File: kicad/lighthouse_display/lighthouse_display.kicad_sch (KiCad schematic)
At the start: 1 part, among them U1 IS31FL3731-SA

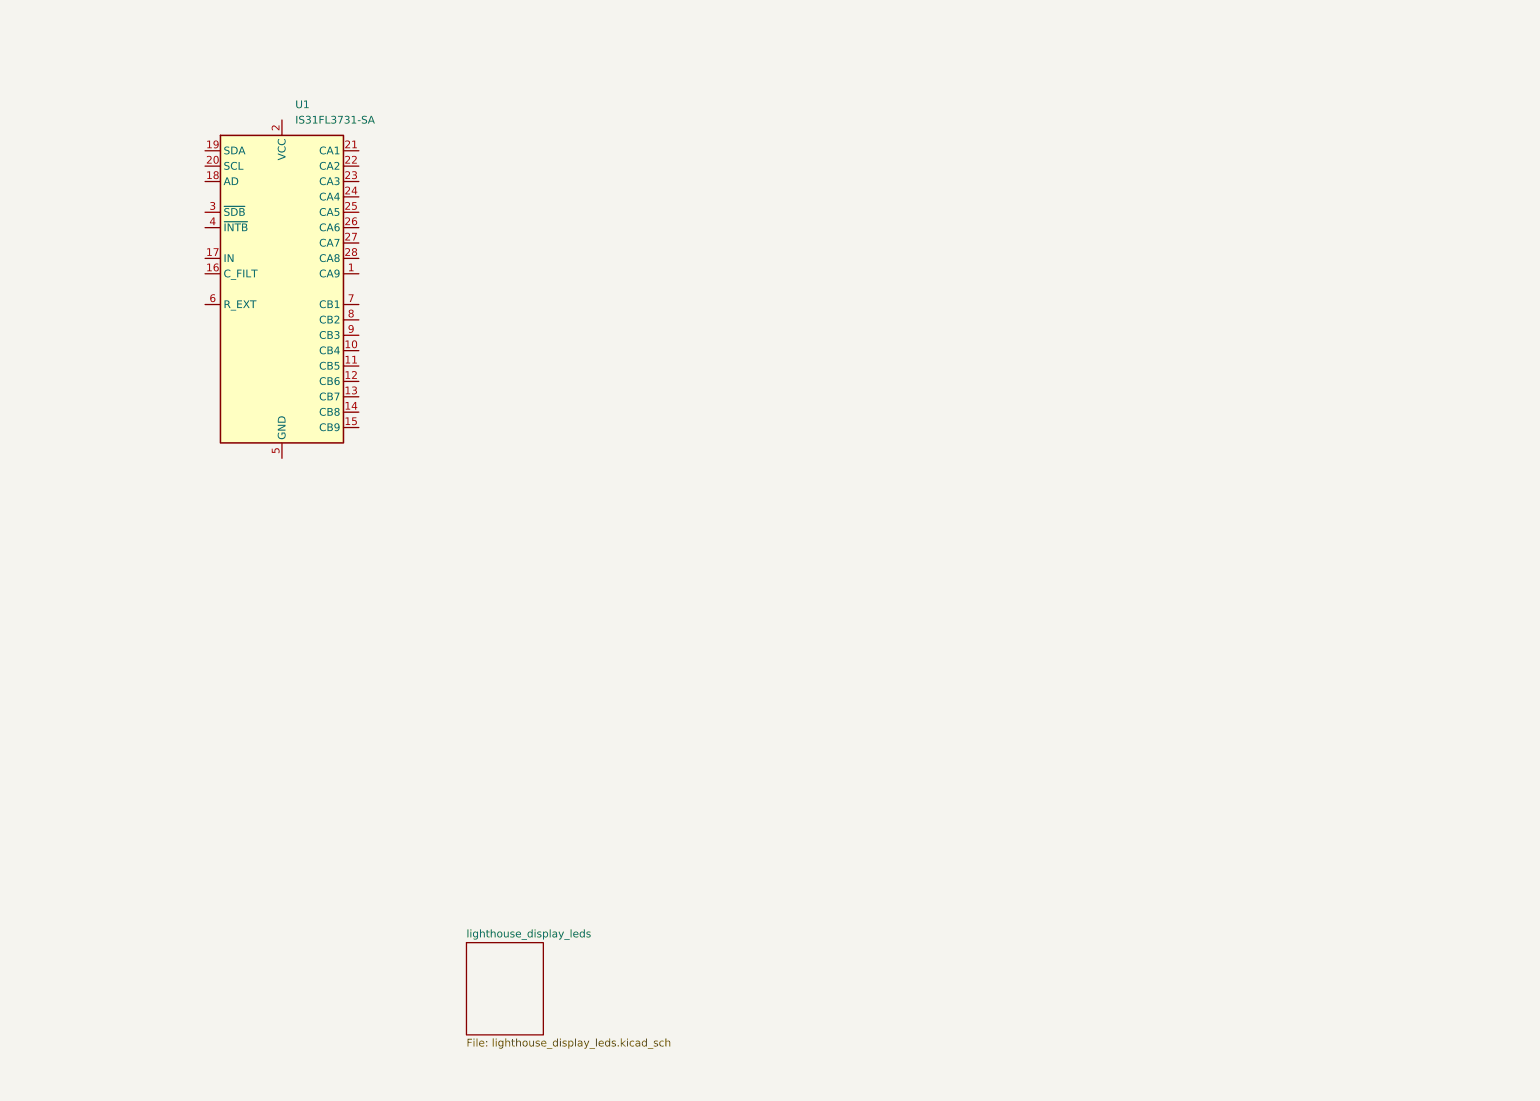
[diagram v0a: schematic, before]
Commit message: white LED driver TPS61176RTER added in lib and sch
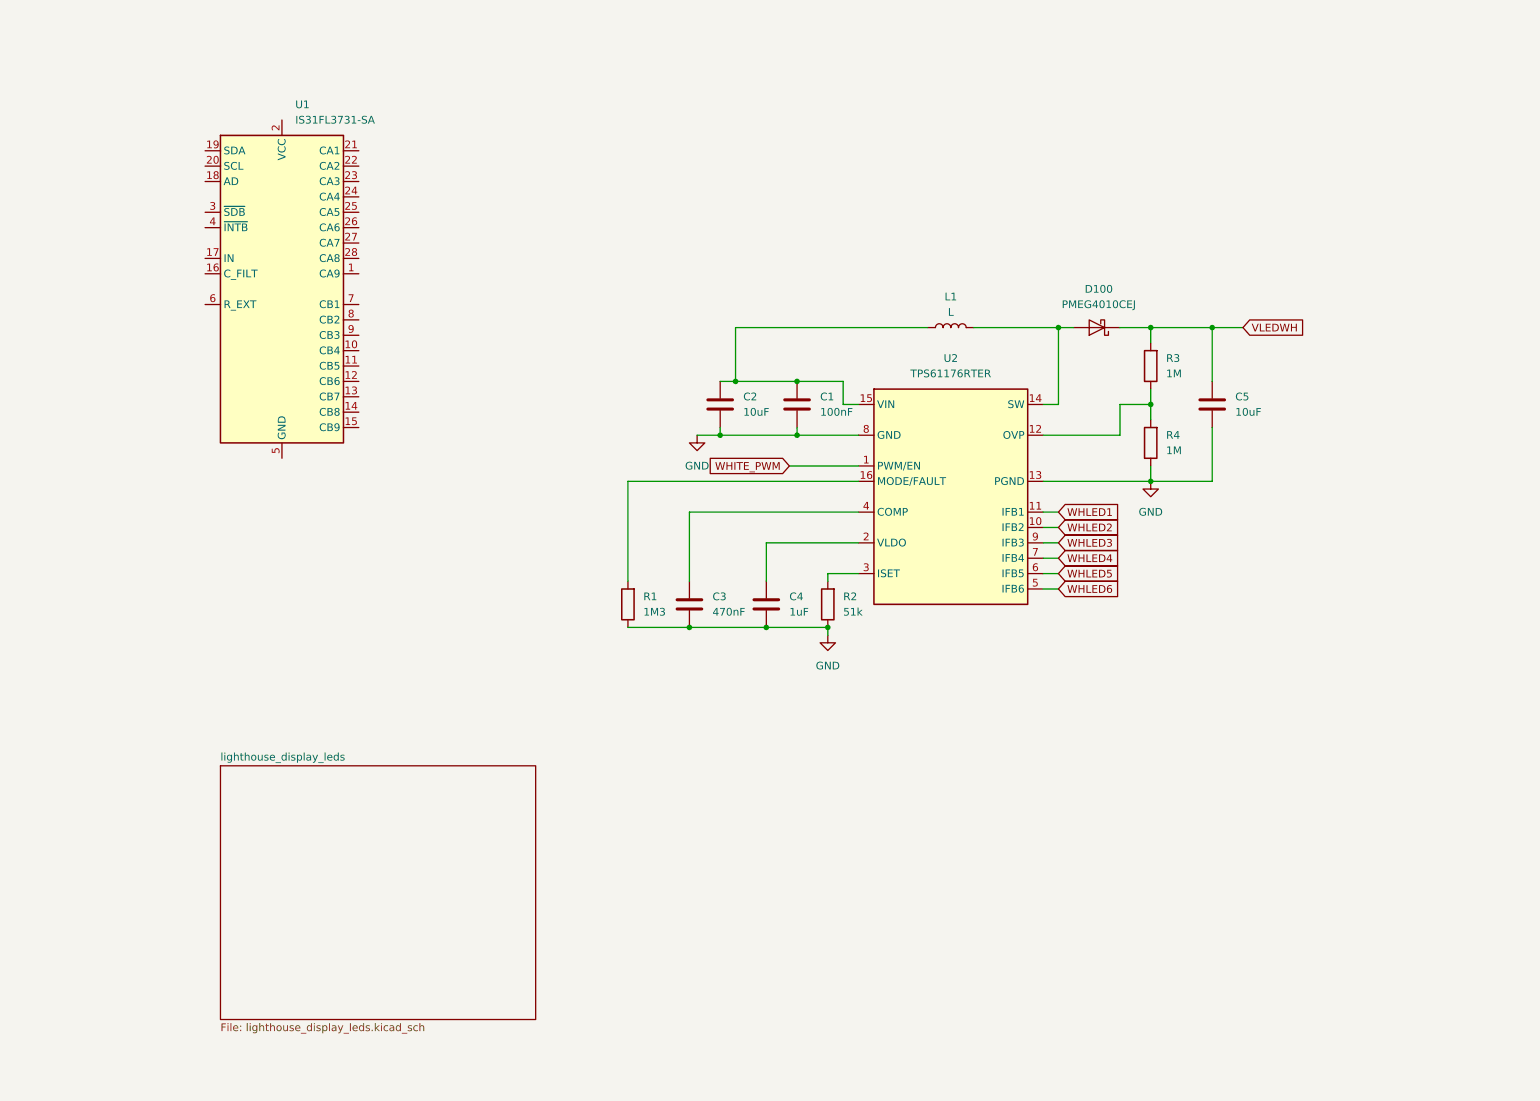
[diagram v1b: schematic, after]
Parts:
- added C1: 100nF, symbol Device:C
- added C2, C5: 10uF, symbol Device:C
- added C3: 470nF, symbol Device:C
- added C4: 1uF, symbol Device:C
- added D100: PMEG4010CEJ, Diode_SMD:D_SOD-323F, symbol Diode:PMEG4010CEJ
- added L1: L, symbol Device:L
- added R1: 1M3, symbol Device:R
- added R2: 51k, symbol Device:R
- added R3, R4: 1M, symbol Device:R
- added U2: TPS61176RTER, symbol lighthouse:TPS61176RTER
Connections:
- new net: R3.1, R4.2, U2.12 (OVP)
- new net: D100.2 (A), L1.2, U2.14 (SW)
- new net: C1.1, C2.1, L1.1, U2.15 (VIN)
- new net: R1.2, U2.16 (MODE/FAULT)
- new net: C4.1, U2.2 (VLDO)
- new net: R2.2, U2.3 (ISET)
- new net: C3.1, U2.4 (COMP)
- new net GND: C1.2, C2.2, C3.2, C4.2, C5.2, R1.1, R2.1, R4.1, U2.13 (PGND), U2.8 (GND)
- new net VLEDWH: C5.1, D100.1 (K), R3.2
- new net WHITE_PWM: U2.1 (PWM/EN)
- new net WHLED1: U2.11 (IFB1)
- new net WHLED2: U2.10 (IFB2)
- new net WHLED3: U2.9 (IFB3)
- new net WHLED4: U2.7 (IFB4)
- new net WHLED5: U2.6 (IFB5)
- new net WHLED6: U2.5 (IFB6)

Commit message: much ado about LEDs :-)
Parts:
- added C1, C6, C8: 100nF, symbol Device:C
- added C7: 10uF, symbol Device:C
- added J1: Conn_01x12_Pin, symbol Connector:Conn_01x12_Pin
- added R10, R11, R5, R8, R9: 1M, symbol Device:R
- added R12: 20k, symbol Device:R
- added R6, R7: 4k7, symbol Device:R
- C11: renamed from C1; value 100nF -> 1uF
- R4: value 1M -> 83k3
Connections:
- net GND: now also U1.5 (GND), C1.2, C6.2, C7.2, C8.2, J1.12 (Pin_12), J1.2 (Pin_2), J1.4 (Pin_4), R10.1, R11.1, R12.1, R9.1
- net WHITE_PWM: now also J1.9 (Pin_9)
- net +3.3V: now reaches C11.1, U2.15 (VIN)
- net +3.3V: now also J1.3 (Pin_3), R5.2, R6.2, R7.2, R8.2; no longer C2.1, L1.1
- net CA9: now reaches U1.1 (CA9)
- net CB4: now reaches U1.10 (CB4)
- net CB5: now reaches U1.11 (CB5)
- net CB6: now reaches U1.12 (CB6)
- net CB7: now reaches U1.13 (CB7)
- net CB8: now reaches U1.14 (CB8)
- net CB9: now reaches U1.15 (CB9)
- net at U1.16 (C_FILT): now also C6.1
- net at U1.17 (IN): now also R11.2
- net at U1.18 (AD): now also R10.2, R8.1
- net SDA: now reaches U1.19 (SDA)
- net SDA: now also J1.5 (Pin_5), R7.1
- net +BATT: now reaches U1.2 (VCC)
- net +BATT: now also C2.1, L1.1, C1.1, C7.1, C8.1, J1.1 (Pin_1)
- net SCL: now reaches U1.20 (SCL)
- net SCL: now also J1.6 (Pin_6), R6.1
- net CA1: now reaches U1.21 (CA1)
- net CA2: now reaches U1.22 (CA2)
- net CA3: now reaches U1.23 (CA3)
- net CA4: now reaches U1.24 (CA4)
- net CA5: now reaches U1.25 (CA5)
- net CA6: now reaches U1.26 (CA6)
- net CA7: now reaches U1.27 (CA7)
- net CA8: now reaches U1.28 (CA8)
- net ~{SDB}: now reaches U1.3 (~{SDB})
- net ~{SDB}: now also J1.7 (Pin_7), R9.2
- net ~{INTB}: now reaches U1.4 (~{INTB})
- net ~{INTB}: now also J1.8 (Pin_8), R5.1
- net at U1.6 (R_EXT): now also R12.2
- net CB1: now reaches U1.7 (CB1)
- net CB2: now reaches U1.8 (CB2)
- net CB3: now reaches U1.9 (CB3)
- no-connect marks 0 -> 2
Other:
- note added: "6 white LEDs in series @ 20 mA -> 3.25 V VOUT 6*3.25 V = 19.5 V, VFB = 1.5 VOUT = (Rupper/Rlower + 1) * 1.5 V Rlower = Rupper / (VOUT/VFB - 1) = 83.33k @ Rupper = 1M"
- note added: "AD: set I2C address"
- moved on the sheet: C11, C2, C3, C4, C5, D100, L1, R1, R2, R3, R4, U1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

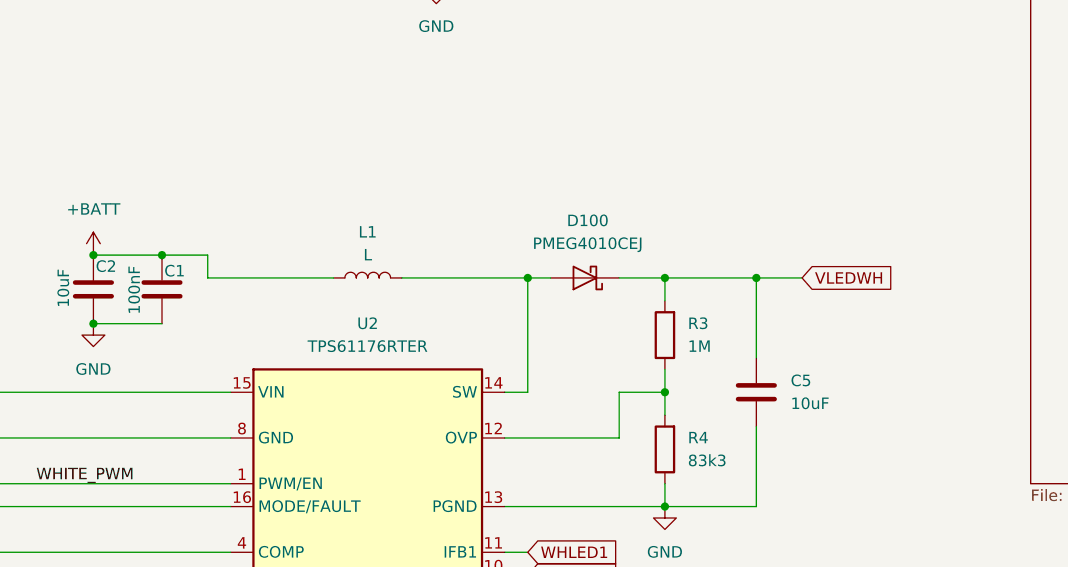
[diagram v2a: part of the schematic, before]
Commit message: sch: all leds connected, also set all footprints
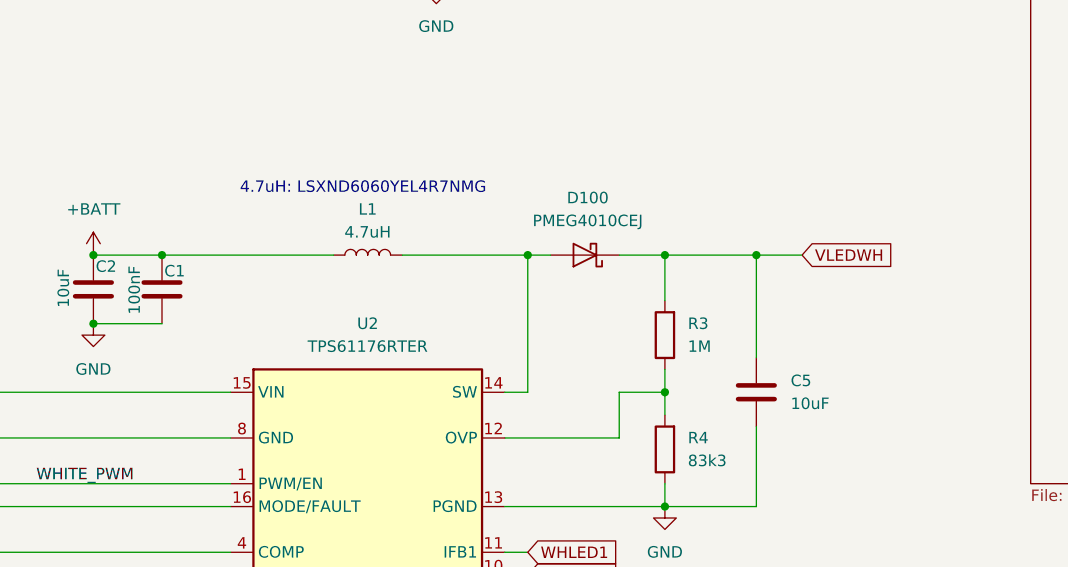
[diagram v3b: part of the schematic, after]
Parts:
- C1, C3, C6, C8: footprint (none) -> Capacitor_SMD:C_0603_1608Metric_Pad1.08x0.95mm_HandSolder
- C11, C2, C4, C5, C7: footprint (none) -> Capacitor_SMD:C_0805_2012Metric_Pad1.18x1.45mm_HandSolder
- J1: footprint (none) -> Connector_PinHeader_1.27mm:PinHeader_1x12_P1.27mm_Vertical
- L1: value L -> 4.7uH; footprint (none) -> Inductor_SMD:L_Taiyo-Yuden_NR-60xx_HandSoldering
- R1, R10, R11, R12, R2, R3, R4, R5, R6, R7, R8, R9: footprint (none) -> Resistor_SMD:R_0603_1608Metric_Pad0.98x0.95mm_HandSolder
- U2: footprint (none) -> Package_DFN_QFN:Texas_RTE0016D_WQFN-16-1EP_3x3mm_P0.5mm_EP0.8x0.8mm
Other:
- note added: "4.7uH: LSXND6060YEL4R7NMG"
- moved on the sheet: D100, L1
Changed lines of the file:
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@@
 	)
 	(junction
-		(at 134.62 129.54)
+		(at 134.62 127)
 		(diameter 0)
 		(color 0 0 0 0)
@@
 	)
 	(junction
-		(at 119.38 129.54)
+		(at 119.38 127)
 		(diameter 0)
 		(color 0 0 0 0)
@@
 	)
 	(junction
-		(at 144.78 129.54)
+		(at 144.78 127)
 		(diameter 0)
 		(color 0 0 0 0)
@@
 	(wire
 		(pts
-			(xy 83.82 129.54) (xy 83.82 127)
-		)
-		(stroke
-			(width 0)
-			(type default)
-		)
-	)
-	(wire
-		(pts
 			(xy 86.36 50.8) (xy 96.52 50.8)
 		)
@@
 	(wire
 		(pts
-			(xy 134.62 129.54) (xy 134.62 132.08)
+			(xy 134.62 127) (xy 134.62 132.08)
+		)
+		(stroke
+			(width 0)
+			(type default)
+		)
+	)
+	(wire
+		(pts
+			(xy 78.74 127) (xy 97.79 127)
 		)
 		(stroke
@@
 	(wire
 		(pts
-			(xy 144.78 129.54) (xy 149.86 129.54)
+			(xy 144.78 127) (xy 149.86 127)
 		)
 		(stroke
@@
 	(wire
 		(pts
-			(xy 83.82 129.54) (xy 97.79 129.54)
-		)
-		(stroke
-			(width 0)
-			(type default)
-		)
-	)
-	(wire
-		(pts
 			(xy 116.84 165.1) (xy 119.38 165.1)
 		)
@@
 	(wire
 		(pts
-			(xy 144.78 138.43) (xy 144.78 129.54)
+			(xy 144.78 138.43) (xy 144.78 127)
 		)
 		(stroke
@@
 	(wire
 		(pts
-			(xy 129.54 129.54) (xy 134.62 129.54)
+			(xy 129.54 127) (xy 134.62 127)
 		)
 		(stroke
@@
 	(wire
 		(pts
-			(xy 119.38 129.54) (xy 121.92 129.54)
+			(xy 119.38 127) (xy 121.92 127)
 		)
 		(stroke
@@
 	(wire
 		(pts
-			(xy 83.82 127) (xy 78.74 127)
-		)
-		(stroke
-			(width 0)
-			(type default)
-		)
-	)
-	(wire
-		(pts
 			(xy 88.9 78.74) (xy 88.9 82.55)
 		)
@@
 	(wire
 		(pts
-			(xy 144.78 129.54) (xy 134.62 129.54)
+			(xy 144.78 127) (xy 134.62 127)
 		)
 		(stroke
@@
 	(wire
 		(pts
-			(xy 119.38 129.54) (xy 119.38 142.24)
+			(xy 119.38 127) (xy 119.38 142.24)
 		)
 		(stroke
@@
 	(wire
 		(pts
-			(xy 105.41 129.54) (xy 119.38 129.54)
+			(xy 105.41 127) (xy 119.38 127)
 		)
 		(stroke
@@
 		)
 	)
+	(text "4.7uH: LSXND6060YEL4R7NMG "
+		(exclude_from_sim no)
+		(at 101.092 119.634 0)
+		(effects
+			(font
+				(size 1.27 1.27)
+			)
+		)
+	)
 	(text "6 white LEDs in series @ 20 mA -> 3.25 V\nVOUT 6*3.25 V = 19.5 V, VFB = 1.5\nVOUT = (Rupper/Rlower + 1) * 1.5 V\nRlower = Rupper / (VOUT/VFB - 1) = 83.33k @ Rupper = 1M"
 		(exclude_from_sim no)
@@
 	(global_label "VLEDWH"
 		(shape input)
-		(at 149.86 129.54 0)
+		(at 149.86 127 0)
 		(fields_autoplaced yes)
 		(effects
@@
 		)
 		(property "Intersheetrefs" "${INTERSHEET_REFS}"
-			(at 160.1628 129.54 0)
+			(at 160.1628 127 0)
 			(effects
 				(font
@@
 			)
 		)
-		(property "Footprint" ""
+		(property "Footprint" "Resistor_SMD:R_0603_1608Metric_Pad0.98x0.95mm_HandSolder"
 			(at 80.518 35.56 90)
 			(effects
@@
 			)
 		)
-		(property "Footprint" ""
+		(property "Footprint" "Package_DFN_QFN:Texas_RTE0016D_WQFN-16-1EP_3x3mm_P0.5mm_EP0.8x0.8mm"
 			(at 101.6 137.16 0)
 			(effects
@@
 			)
 		)
-		(property "Footprint" ""
+		(property "Footprint" "Resistor_SMD:R_0603_1608Metric_Pad0.98x0.95mm_HandSolder"
 			(at 83.058 35.56 90)
 			(effects
@@
 			)
 		)
-		(property "Footprint" ""
+		(property "Footprint" "Resistor_SMD:R_0603_1608Metric_Pad0.98x0.95mm_HandSolder"
 			(at 88.138 35.56 90)
 			(effects
@@
 			)
 		)
-		(property "Footprint" ""
+		(property "Footprint" "Capacitor_SMD:C_0805_2012Metric_Pad1.18x1.45mm_HandSolder"
 			(at 44.1452 146.05 0)
 			(effects
@@
 			)
 		)
-		(property "Footprint" ""
+		(property "Footprint" "Capacitor_SMD:C_0603_1608Metric_Pad1.08x0.95mm_HandSolder"
 			(at 59.3852 179.07 0)
 			(effects
@@
 			)
 		)
-		(property "Footprint" ""
+		(property "Footprint" "Connector_PinHeader_1.27mm:PinHeader_1x12_P1.27mm_Vertical"
 			(at 45.72 48.26 0)
 			(effects
@@
 			)
 		)
-		(property "Footprint" ""
+		(property "Footprint" "Capacitor_SMD:C_0805_2012Metric_Pad1.18x1.45mm_HandSolder"
 			(at 97.4852 38.1 0)
 			(effects
@@
 			)
 		)
-		(property "Footprint" ""
+		(property "Footprint" "Capacitor_SMD:C_0805_2012Metric_Pad1.18x1.45mm_HandSolder"
 			(at 72.0852 179.07 0)
 			(effects
@@
 			)
 		)
-		(property "Footprint" ""
+		(property "Footprint" "Resistor_SMD:R_0603_1608Metric_Pad0.98x0.95mm_HandSolder"
 			(at 88.138 74.93 90)
 			(effects
@@
 			)
 		)
-		(property "Footprint" ""
+		(property "Footprint" "Resistor_SMD:R_0603_1608Metric_Pad0.98x0.95mm_HandSolder"
 			(at 93.218 74.93 90)
 			(effects
@@
 			)
 		)
-		(property "Footprint" ""
+		(property "Footprint" "Capacitor_SMD:C_0603_1608Metric_Pad1.08x0.95mm_HandSolder"
 			(at 79.7052 134.62 0)
 			(effects
@@
 			)
 		)
-		(property "Footprint" ""
+		(property "Footprint" "Resistor_SMD:R_0603_1608Metric_Pad0.98x0.95mm_HandSolder"
 			(at 136.398 135.89 90)
 			(effects
@@
 			)
 		)
-		(property "Footprint" ""
+		(property "Footprint" "Capacitor_SMD:C_0603_1608Metric_Pad1.08x0.95mm_HandSolder"
 			(at 79.7052 80.01 0)
 			(effects
@@
 			)
 		)
-		(property "Footprint" ""
+		(property "Footprint" "Resistor_SMD:R_0603_1608Metric_Pad0.98x0.95mm_HandSolder"
 			(at 85.598 74.93 90)
 			(effects
@@
 			)
 		)
-		(property "Footprint" ""
+		(property "Footprint" "Resistor_SMD:R_0603_1608Metric_Pad0.98x0.95mm_HandSolder"
 			(at 85.598 35.56 90)
 			(effects
@@
 			)
 		)
-		(property "Footprint" ""
+		(property "Footprint" "Capacitor_SMD:C_0805_2012Metric_Pad1.18x1.45mm_HandSolder"
 			(at 72.0852 134.62 0)
 			(effects
@@
 			)
 		)
-		(property "Footprint" ""
+		(property "Footprint" "Capacitor_SMD:C_0603_1608Metric_Pad1.08x0.95mm_HandSolder"
 			(at 105.1052 38.1 0)
 			(effects
@@
 	(symbol
 		(lib_id "Device:L")
-		(at 101.6 129.54 90)
+		(at 101.6 127 90)
 		(unit 1)
 		(exclude_from_sim no)
@@
 		(fields_autoplaced yes)
 		(property "Reference" "L1"
-			(at 101.6 124.46 90)
+			(at 101.6 121.92 90)
 			(effects
 				(font
@@
 			)
 		)
-		(property "Value" "L"
-			(at 101.6 127 90)
+		(property "Value" "4.7uH"
+			(at 101.6 124.46 90)
 			(effects
 				(font
@@
 			)
 		)
-		(property "Footprint" ""
-			(at 101.6 129.54 0)
+		(property "Footprint" "Inductor_SMD:L_Taiyo-Yuden_NR-60xx_HandSoldering"
+			(at 101.6 127 0)
 			(effects
 				(font
@@
 		)
 		(property "Datasheet" "~"
-			(at 101.6 129.54 0)
+			(at 101.6 127 0)
 			(effects
 				(font
@@
 		)
 		(property "Description" "Inductor"
-			(at 101.6 129.54 0)
+			(at 101.6 127 0)
 			(effects
 				(font
@@
 			)
 		)
-		(property "Footprint" ""
+		(property "Footprint" "Resistor_SMD:R_0603_1608Metric_Pad0.98x0.95mm_HandSolder"
 			(at 136.398 148.59 90)
 			(effects
@@
 			)
 		)
-		(property "Footprint" ""
+		(property "Footprint" "Resistor_SMD:R_0603_1608Metric_Pad0.98x0.95mm_HandSolder"
 			(at 50.038 175.26 90)
 			(effects
@@
 			)
 		)
-		(property "Footprint" ""
+		(property "Footprint" "Capacitor_SMD:C_0805_2012Metric_Pad1.18x1.45mm_HandSolder"
 			(at 145.7452 146.05 0)
 			(effects
@@
 			)
 		)
-		(property "Footprint" ""
+		(property "Footprint" "Resistor_SMD:R_0603_1608Metric_Pad0.98x0.95mm_HandSolder"
 			(at 83.058 175.26 90)
 			(effects
@@
 			)
 		)
-		(property "Footprint" ""
+		(property "Footprint" "Resistor_SMD:R_0603_1608Metric_Pad0.98x0.95mm_HandSolder"
 			(at 90.678 74.93 90)
 			(effects
@@
 	(symbol
 		(lib_id "Diode:PMEG4010CEJ")
-		(at 125.73 129.54 180)
+		(at 125.73 127 180)
 		(unit 1)
 		(exclude_from_sim no)
@@
 		(fields_autoplaced yes)
 		(property "Reference" "D100"
-			(at 126.0475 123.19 0)
+			(at 126.0475 120.65 0)
 			(effects
 				(font
@@
 		)
 		(property "Value" "PMEG4010CEJ"
-			(at 126.0475 125.73 0)
+			(at 126.0475 123.19 0)
 			(effects
 				(font
@@
 		)
 		(property "Footprint" "Diode_SMD:D_SOD-323F"
-			(at 125.73 125.095 0)
+			(at 125.73 122.555 0)
 			(effects
 				(font
@@
 		)
 		(property "Datasheet" "https://assets.nexperia.com/documents/data-sheet/PMEG4010CEH_PMEG4010CEJ.pdf"
-			(at 125.73 129.54 0)
+			(at 125.73 127 0)
 			(effects
 				(font
@@
 		)
 		(property "Description" "40V, 1A very low Vf MEGA Schottky barrier rectifier, SOD-323F"
-			(at 125.73 129.54 0)
+			(at 125.73 127 0)
 			(effects
 				(font

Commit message: hw display placed red and white leds
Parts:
- added JP1, JP2: Jumper_3_Bridged12, Jumper:SolderJumper-3_P1.3mm_Bridged12_RoundedPad1.0x1.5mm, symbol Jumper:Jumper_3_Bridged12
- J1: footprint Connector_PinHeader_1.27mm:PinHeader_1x12_P1.27mm_Vertical -> lighthouse:con_1x12_1.27mm_long_pads
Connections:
- net +3.3V: now also JP1.1 (A), JP2.1 (A); no longer C11.1, U2.15 (VIN)
- net GND: no longer J1.12 (Pin_12), J1.2 (Pin_2)
- net +BATT renamed +12V
- net +12V: no longer C7.1, C8.1, U1.2 (VCC)
- new net: C11.1, JP1.2 (C), U2.15 (VIN)
- new net: C7.1, C8.1, JP2.2 (C), U1.2 (VCC)
- new net +5V: J1.2 (Pin_2), JP1.3 (B), JP2.3 (B)
- no-connect marks 2 -> 3
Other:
- note added: "+12.0V +5.0V +3.3V"
